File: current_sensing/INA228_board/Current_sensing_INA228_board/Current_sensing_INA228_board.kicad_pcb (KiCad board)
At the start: 2 copper layers, 42.8 x 36.2 mm, 26 parts, among them J1 7461096, J2 7461096, J3 Conn_01x06_Pin, U1 INA228

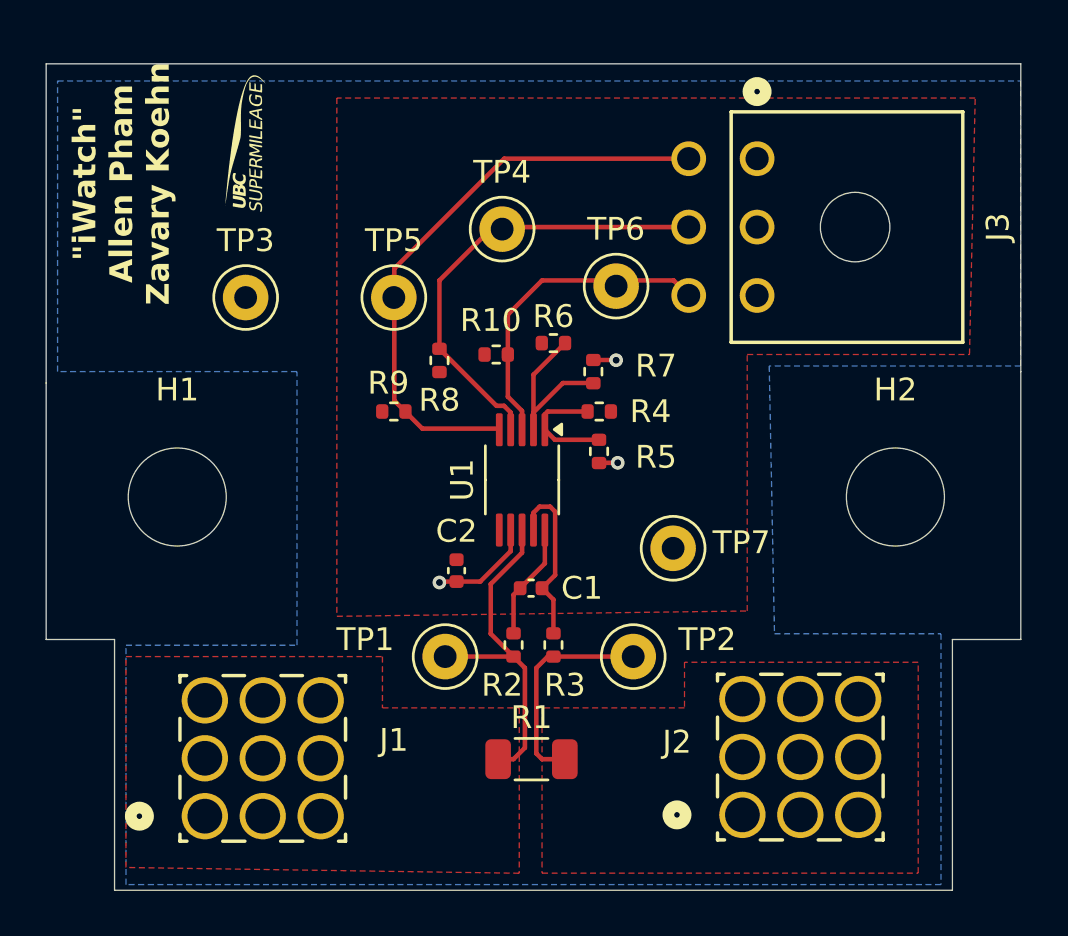
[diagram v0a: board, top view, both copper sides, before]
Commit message: double check on the testpoints, correct labelling
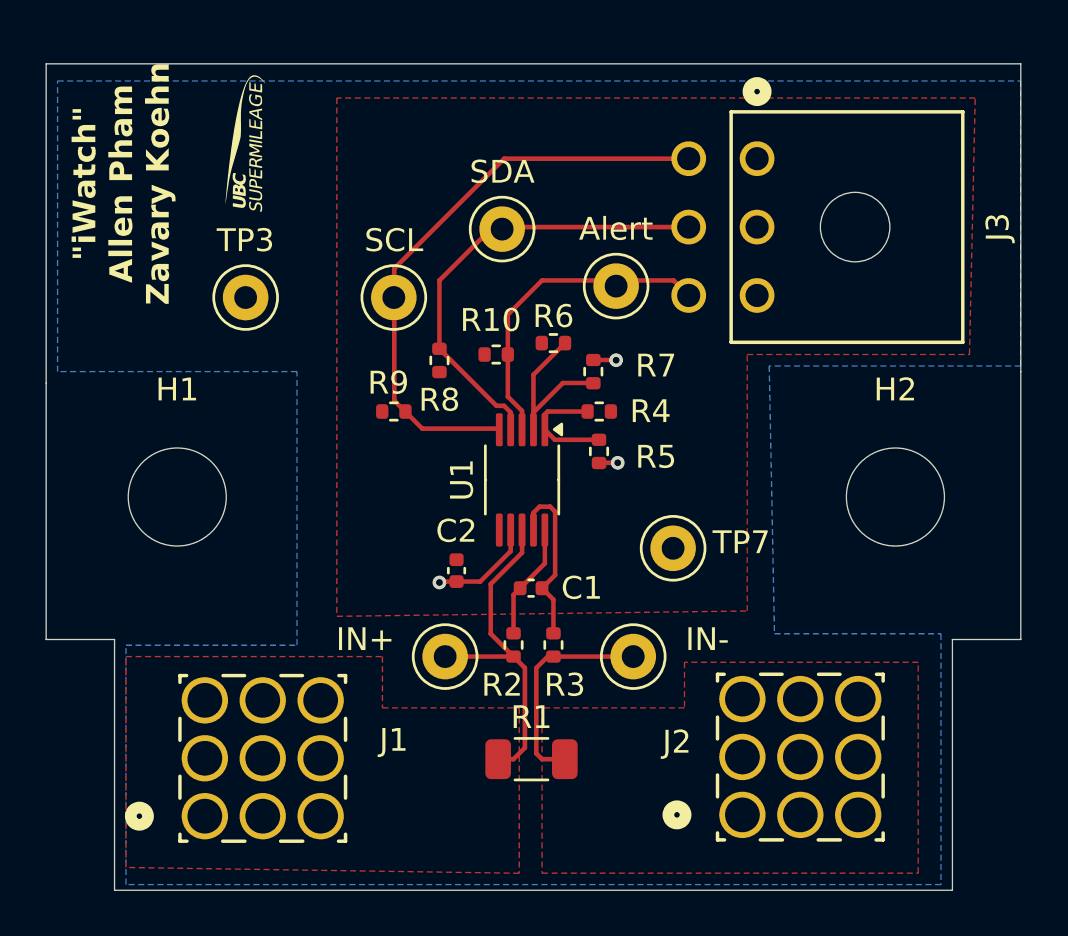
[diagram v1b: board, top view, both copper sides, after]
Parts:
- renumbered TP6 to Alert, TP1 to IN+, TP2 to IN-, TP5 to SCL, TP4 to SDA
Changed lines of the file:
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@@
 		(descr "Keystone THM Miniature Test Point 5000-5004, http://www.keyelco.com/product-pdf.cfm?p=1309")
 		(tags "Through Hole Mount Test Points")
-		(property "Reference" "TP6"
+		(property "Reference" "Alert"
 			(at 0 -2.5 0)
 			(layer "F.SilkS")
@@
 		(descr "Keystone THM Miniature Test Point 5000-5004, http://www.keyelco.com/product-pdf.cfm?p=1309")
 		(tags "Through Hole Mount Test Points")
-		(property "Reference" "TP5"
+		(property "Reference" "SCL"
 			(at 0 -2.5 0)
 			(layer "F.SilkS")
@@
 		(descr "Keystone THM Miniature Test Point 5000-5004, http://www.keyelco.com/product-pdf.cfm?p=1309")
 		(tags "Through Hole Mount Test Points")
-		(property "Reference" "TP4"
+		(property "Reference" "SDA"
 			(at 0 -2.5 0)
 			(layer "F.SilkS")
@@
 		(descr "Keystone THM Miniature Test Point 5000-5004, http://www.keyelco.com/product-pdf.cfm?p=1309")
 		(tags "Through Hole Mount Test Points")
-		(property "Reference" "TP1"
+		(property "Reference" "IN+"
 			(at -3.5 -0.75 0)
 			(layer "F.SilkS")
@@
 		(descr "Keystone THM Miniature Test Point 5000-5004, http://www.keyelco.com/product-pdf.cfm?p=1309")
 		(tags "Through Hole Mount Test Points")
-		(property "Reference" "TP2"
+		(property "Reference" "IN-"
 			(at 3.25 -0.75 0)
 			(layer "F.SilkS")

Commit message: Control Board schematics
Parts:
- J1, J2: footprint ul_7461096:CONN9_1096_WRE -> footprints:CONN9_1096_WRE
- R1: footprint Resistor_SMD:R_1206_3216Metric -> Resistor_SMD:R_0603_1608Metric
- R10, R2, R3, R4, R5, R6, R7, R8, R9: footprint Resistor_SMD:R_0402_1005Metric -> Resistor_SMD:R_0603_1608Metric
- TP7: value 3.3V -> 5V
- renumbered IN+ to TP1, IN- to TP2, SDA to TP4, SCL to TP5, Alert to TP6
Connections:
- net +3.3V renamed +5V
